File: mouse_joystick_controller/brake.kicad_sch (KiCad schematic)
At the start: 5 parts, among them J1 Conn_TERM_HDR_01x02_Pin_3.5MM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, U5 NCR421ZX

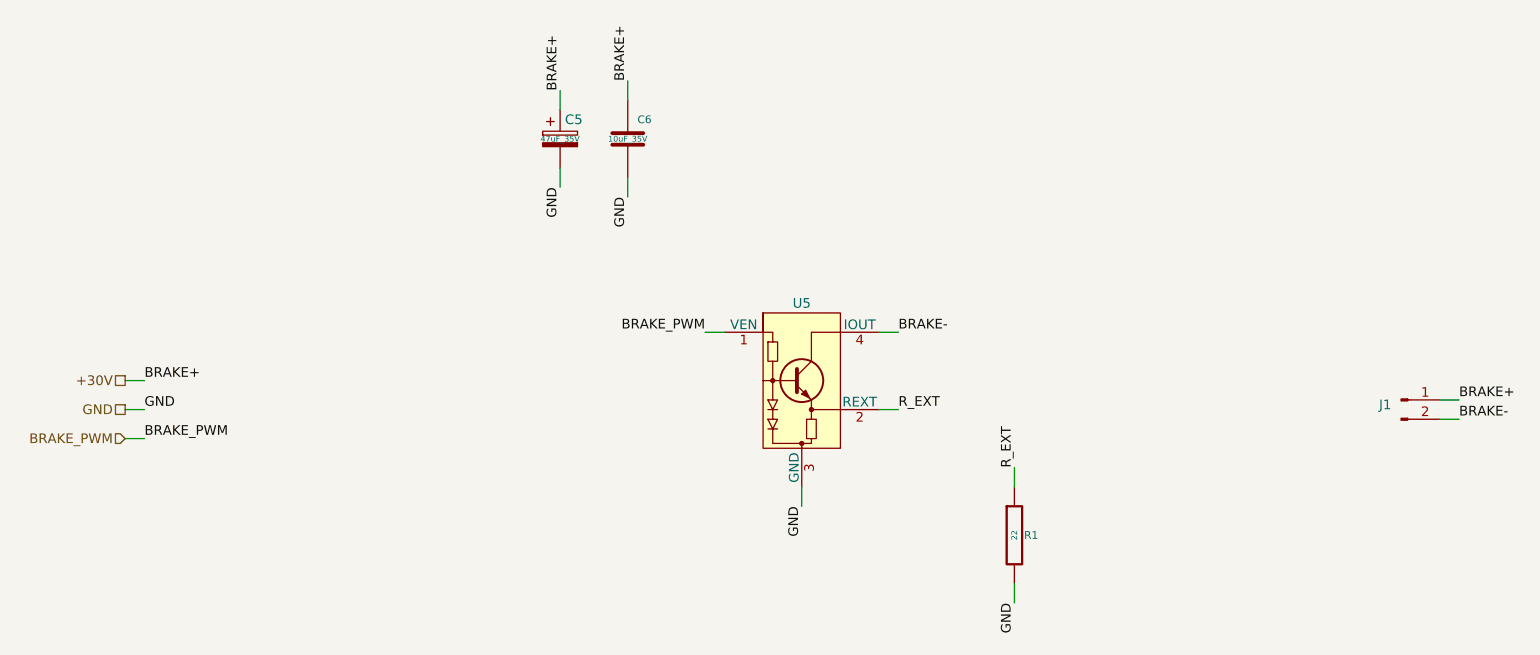
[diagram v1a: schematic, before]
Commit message: Test pin rcpt
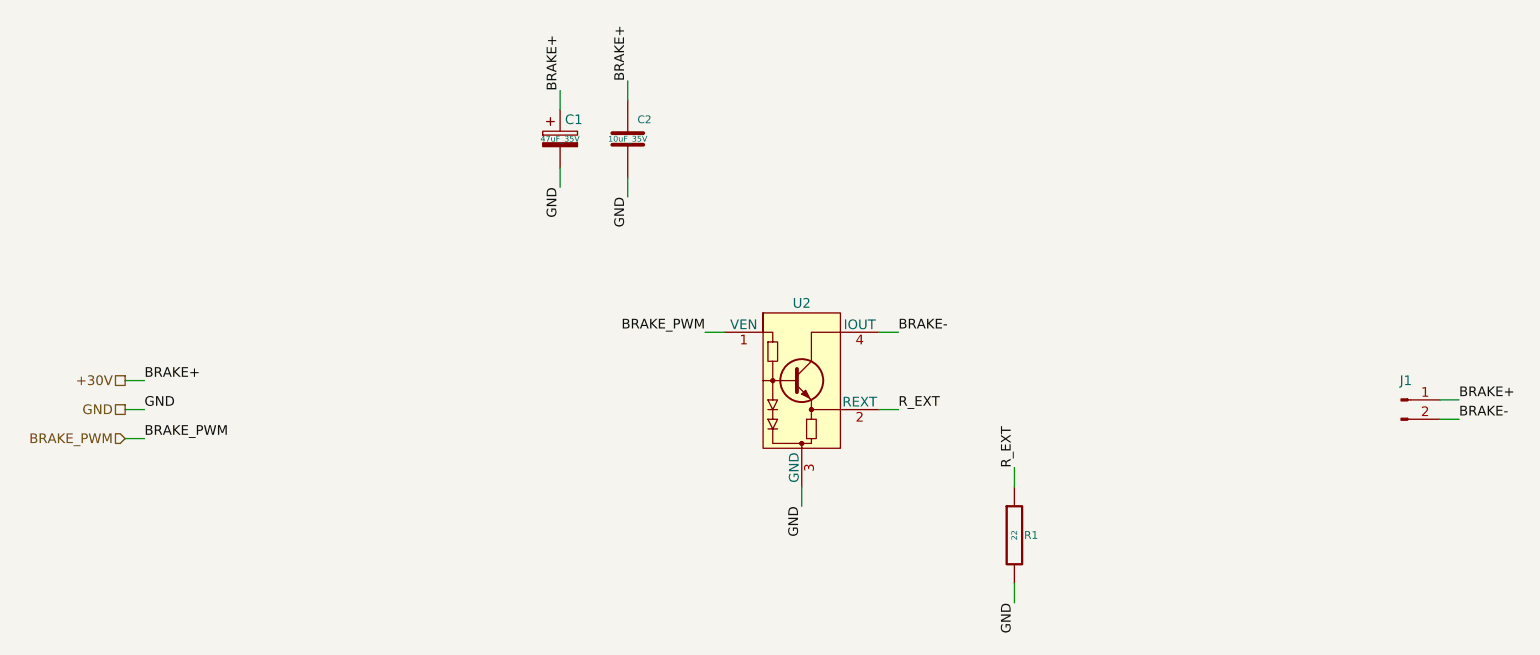
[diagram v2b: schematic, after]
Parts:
- renumbered C5 to C1, C6 to C2, U5 to U2
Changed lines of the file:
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@@
   (title_block
     (title "mouse_joystick_controller")
-    (date "2023-06-07")
+    (date "2023-06-09")
     (rev "2.0")
     (company "Howard Hughes Medical Institute")
@@
   (symbol (lib_id "Janelia:NCR421ZX") (at 135.89 88.9 0) (unit 1)
     (in_bom yes) (on_board yes) (dnp no)
-    (property "Reference" "U5" (at 135.89 78.74 0)
+    (property "Reference" "U2" (at 135.89 78.74 0)
       (effects (font (size 1.27 1.27)))
     )
@@
       (effects (font (size 1.27 1.27)) hide)
     )
+    (property "Sim.Enable" "0" (at 135.89 88.9 0)
+      (effects (font (size 1.27 1.27)) hide)
+    )
     (pin "1")
     (pin "2")
@@
       (project "mouse_joystick_controller"
         (path "/cc457ebc-4af6-4663-b19f-8cb38f061cb4/588c1a3c-052e-4e39-a8d9-29d79b9f5498"
-          (reference "U5") (unit 1)
+          (reference "U2") (unit 1)
         )
       )
@@
   (symbol (lib_id "Janelia:C_10uF_35V_0603") (at 113.03 57.15 0) (unit 1)
     (in_bom yes) (on_board yes) (dnp no)
-    (property "Reference" "C6" (at 114.3 54.61 0)
+    (property "Reference" "C2" (at 114.3 54.61 0)
       (effects (font (size 1.016 1.016)) (justify left))
     )
@@
       (project "mouse_joystick_controller"
         (path "/cc457ebc-4af6-4663-b19f-8cb38f061cb4/588c1a3c-052e-4e39-a8d9-29d79b9f5498"
-          (reference "C6") (unit 1)
+          (reference "C2") (unit 1)
         )
       )
@@
   (symbol (lib_id "Janelia:Conn_TERM_HDR_01x02_Pin_3.5MM_Horizontal") (at 214.63 91.44 0) (unit 1)
     (in_bom yes) (on_board yes) (dnp no) (fields_autoplaced)
-    (property "Reference" "J1" (at 213.36 92.075 0)
-      (effects (font (size 1.27 1.27)) (justify right))
+    (property "Reference" "J1" (at 215.265 88.9 0)
+      (effects (font (size 1.27 1.27)))
     )
     (property "Value" "Conn_TERM_HDR_01x02_Pin_3.5MM_Horizontal" (at 214.63 104.14 0)
@@
     )
     (property "Vendor Part Number" "277-2416-ND" (at 214.63 68.58 0)
+      (effects (font (size 1.27 1.27)) hide)
+    )
+    (property "Sim.Enable" "0" (at 214.63 91.44 0)
       (effects (font (size 1.27 1.27)) hide)
     )
@@
   (symbol (lib_id "Janelia:C_47uF_35V_2917_POL") (at 104.14 57.15 0) (unit 1)
     (in_bom yes) (on_board yes) (dnp no) (fields_autoplaced)
-    (property "Reference" "C5" (at 104.775 54.61 0) (do_not_autoplace)
+    (property "Reference" "C1" (at 104.775 54.61 0) (do_not_autoplace)
       (effects (font (size 1.27 1.27)) (justify left))
     )
@@
       (project "mouse_joystick_controller"
         (path "/cc457ebc-4af6-4663-b19f-8cb38f061cb4/588c1a3c-052e-4e39-a8d9-29d79b9f5498"
-          (reference "C5") (unit 1)
-        )
-      )
+          (reference "C1") (unit 1)
+        )
+      )

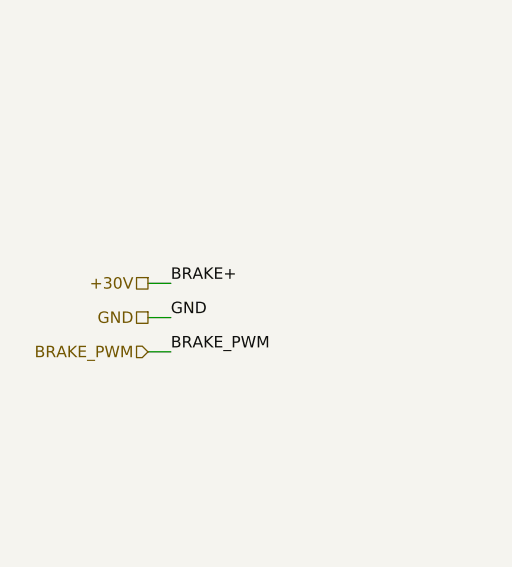
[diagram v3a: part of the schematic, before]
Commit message: Update to kicad 7.0.8
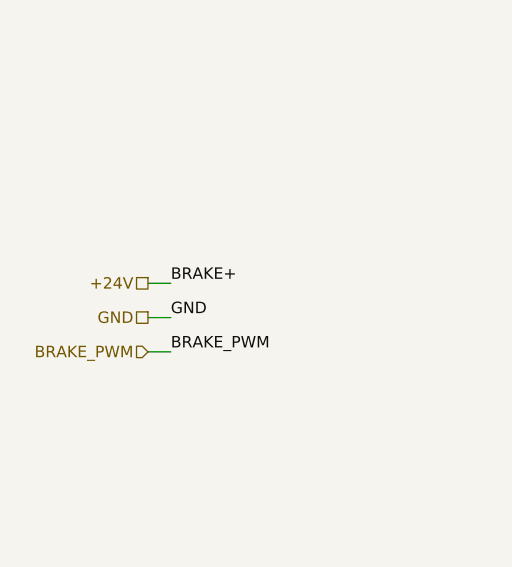
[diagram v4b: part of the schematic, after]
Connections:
- net +30V renamed +24V
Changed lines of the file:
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@@
   (title_block
     (title "mouse_joystick_controller")
-    (date "2023-07-12")
+    (date "2023-10-13")
     (rev "2.0")
     (company "Howard Hughes Medical Institute")
@@
     (effects (font (size 1.27 1.27)) (justify right))
   )
-  (hierarchical_label "+30V" (shape passive) (at 46.99 88.9 180) (fields_autoplaced)
+  (hierarchical_label "+24V" (shape passive) (at 46.99 88.9 180) (fields_autoplaced)
     (effects (font (size 1.27 1.27)) (justify right))
   )
